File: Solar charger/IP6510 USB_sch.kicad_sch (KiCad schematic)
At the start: 1 part, among them U6 IP6510

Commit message: board compelet
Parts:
- added C17: 22u, Capacitor_SMD:C_0805_2012Metric, symbol Device:C
- added C18: 1u, Capacitor_SMD:C_0805_2012Metric, symbol Device:C
- added C19: 1n, Capacitor_SMD:C_0805_2012Metric, symbol Device:C
- added C20: 0.1u, Capacitor_SMD:C_0805_2012Metric, symbol Device:C
- added C21: 220u, Capacitor_THT:CP_Radial_D6.3mm_P2.50mm, symbol Device:C_Polarized
- added C22: 10u, Capacitor_SMD:C_0805_2012Metric, symbol Device:C
- added L2: L, Inductor_SMD:L_10.4x10.4_H4.8, symbol Device:L
- added R13: 2, Resistor_SMD:R_0805_2012Metric, symbol Device:R_US
- added R14: 3.3k, Resistor_SMD:R_0805_2012Metric, symbol Device:R_US
- U6: footprint Package_SO:SOIC-8-1EP_3.9x4.9mm_P1.27mm_EP2.29x3mm_ThermalVias -> 1Resouce:SOIC-8-1EP_3.9x4.9mm_P1.27mm_EP2.29x3mm_ThermalVias
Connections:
- net GND: now also C17.2, C18.2, C19.2, C21.2, C22.2, R14.2
- net Power Input: now also C17.1, C18.1
- net Power Output: now also C21.1, C22.1, L2.2, R14.1
- net at U6.3 (SW): now also C20.1, L2.1, R13.1
- net at U6.4 (BST): now also C20.2
- new net: C19.1, R13.2

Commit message: 增加新回測報告，單獨IP6050 BOM表
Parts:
- L2: value L -> 22u
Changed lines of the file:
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@@
     (in_bom yes) (on_board yes) (fields_autoplaced)
     (property "Reference" "L2" (id 0) (at 140.97 55.88 90))
-    (property "Value" "L" (id 1) (at 140.97 58.42 90))
+    (property "Value" "22u" (id 1) (at 140.97 58.42 90))
     (property "Footprint" "Inductor_SMD:L_10.4x10.4_H4.8" (id 2) (at 140.97 62.23 0)
       (effects (font (size 1.27 1.27)) hide)
@@
     (pin "1")
   )
+  (sheet_instances
+    (path "/" (page "1"))
+  )
+  (symbol_instances
+    (path "/ec1175d1-1bab-4b8d-ae80-0cf784214bf8"
+      (reference "#PWR07") (unit 1) (value "GND") (footprint "")
+    )
+    (path "/5403a568-63d9-40cc-a753-fb6316d05a55"
+      (reference "C17") (unit 1) (value "22u") (footprint "Capacitor_SMD:C_0805_2012Metric")
+    )
+    (path "/16e5afc8-ff48-4a61-aebb-707d83932b6e"
+      (reference "C18") (unit 1) (value "1u") (footprint "Capacitor_SMD:C_0805_2012Metric")
+    )
+    (path "/c1da5aff-79c8-4d1c-ba9a-24c37276a15a"
+      (reference "C19") (unit 1) (value "1n") (footprint "Capacitor_SMD:C_0805_2012Metric")
+    )
+    (path "/a19c7708-07b9-4e7c-af96-e793517d2808"
+      (reference "C20") (unit 1) (value "0.1u") (footprint "Capacitor_SMD:C_0805_2012Metric")
+    )
+    (path "/4bef6a33-e19b-415f-bbcc-7e54b70d75ed"
+      (reference "C21") (unit 1) (value "220u") (footprint "Capacitor_THT:CP_Radial_D6.3mm_P2.50mm")
+    )
+    (path "/512978ce-74f7-4676-9cdc-95706ce5f098"
+      (reference "C22") (unit 1) (value "10u") (footprint "Capacitor_SMD:C_0805_2012Metric")
+    )
+    (path "/1b7abc99-ad47-483d-8f4a-7ebca9268ba0"
+      (reference "L2") (unit 1) (value "22u") (footprint "Inductor_SMD:L_10.4x10.4_H4.8")
+    )
+    (path "/5b422114-532e-4775-be5f-7c65f529b745"
+      (reference "R13") (unit 1) (value "2") (footprint "Resistor_SMD:R_0805_2012Metric")
+    )
+    (path "/571de38c-5803-4614-b839-1f13c9da8365"
+      (reference "R14") (unit 1) (value "3.3k") (footprint "Resistor_SMD:R_0805_2012Metric")
+    )
+    (path "/2df9c9f8-559b-4185-a144-00c57204afb9"
+      (reference "U6") (unit 1) (value "IP6510") (footprint "1Resouce:SOIC-8-1EP_3.9x4.9mm_P1.27mm_EP2.29x3mm_ThermalVias")
+    )
+  )
 )

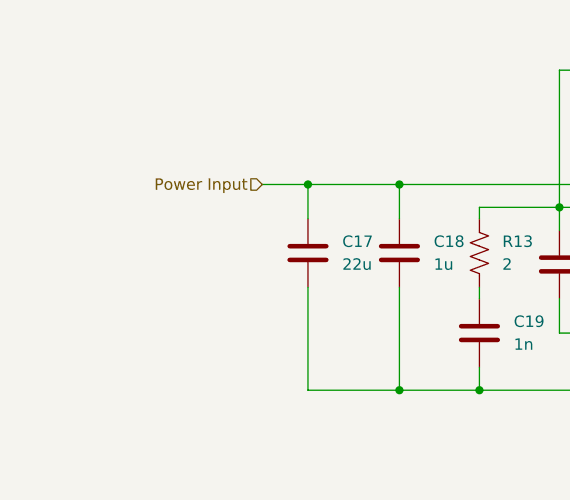
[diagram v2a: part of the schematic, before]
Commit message: 增加電路圖PDF，新增修改一些元件
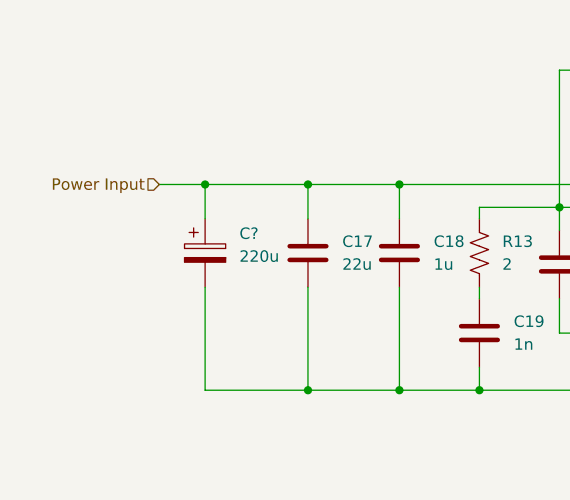
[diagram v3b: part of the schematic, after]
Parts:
- added C?: 220u, Capacitor_THT:CP_Radial_D6.3mm_P2.50mm, symbol Device:C_Polarized
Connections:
- net GND: now also C?.2
- net Power Input: now also C?.1
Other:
- title: (none) -> 8V IN ip6510 Type-c OUT
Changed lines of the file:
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@@
 (kicad_sch (version 20211123) (generator eeschema)
   (paper "A4")
+  (title_block
+    (title "8V IN ip6510 Type-c OUT")
+  )
   (junction (at 146.05 64.77) (diameter 0) (color 0 0 0 0)
   )
+  (junction (at 78.74 97.79) (diameter 0) (color 0 0 0 0)
+  )
   (junction (at 88.9 97.79) (diameter 0) (color 0 0 0 0)
   )
@@
   (junction (at 162.56 97.79) (diameter 0) (color 0 0 0 0)
   )
+  (junction (at 67.31 74.93) (diameter 0) (color 0 0 0 0)
+  )
   (junction (at 162.56 64.77) (diameter 0) (color 0 0 0 0)
   )
@@
     (stroke (width 0) (type default) (color 0 0 0 0))
   )
-  (wire (pts (xy 73.66 74.93) (xy 78.74 74.93))
+  (wire (pts (xy 62.23 74.93) (xy 67.31 74.93))
     (stroke (width 0) (type default) (color 0 0 0 0))
   )
@@
     (stroke (width 0) (type default) (color 0 0 0 0))
   )
+  (wire (pts (xy 67.31 74.93) (xy 78.74 74.93))
+    (stroke (width 0) (type default) (color 0 0 0 0))
+  )
   (wire (pts (xy 88.9 97.79) (xy 97.79 97.79))
     (stroke (width 0) (type default) (color 0 0 0 0))
@@
     (stroke (width 0) (type default) (color 0 0 0 0))
   )
+  (wire (pts (xy 67.31 86.36) (xy 67.31 97.79))
+    (stroke (width 0) (type default) (color 0 0 0 0))
+  )
   (wire (pts (xy 146.05 64.77) (xy 151.13 64.77))
     (stroke (width 0) (type default) (color 0 0 0 0))
@@
     (stroke (width 0) (type default) (color 0 0 0 0))
   )
+  (wire (pts (xy 67.31 74.93) (xy 67.31 78.74))
+    (stroke (width 0) (type default) (color 0 0 0 0))
+  )
   (wire (pts (xy 172.72 64.77) (xy 177.8 64.77))
     (stroke (width 0) (type default) (color 0 0 0 0))
@@
     (stroke (width 0) (type default) (color 0 0 0 0))
   )
+  (wire (pts (xy 67.31 97.79) (xy 78.74 97.79))
+    (stroke (width 0) (type default) (color 0 0 0 0))
+  )
   (wire (pts (xy 106.68 77.47) (xy 106.68 62.23))
     (stroke (width 0) (type default) (color 0 0 0 0))
@@
     (stroke (width 0) (type default) (color 0 0 0 0))
   )
-  (hierarchical_label "Power Input" (shape input) (at 73.66 74.93 180)
+  (hierarchical_label "Power Input" (shape input) (at 62.23 74.93 180)
     (effects (font (size 1.27 1.27)) (justify right))
   )
@@
     (pin "1")
   )
+  (symbol (lib_id "Device:C_Polarized") (at 67.31 82.55 0) (unit 1)
+    (in_bom yes) (on_board yes) (fields_autoplaced)
+    (property "Reference" "C?" (id 0) (at 71.12 80.3909 0)
+      (effects (font (size 1.27 1.27)) (justify left))
+    )
+    (property "Value" "220u" (id 1) (at 71.12 82.9309 0)
+      (effects (font (size 1.27 1.27)) (justify left))
+    )
+    (property "Footprint" "Capacitor_THT:CP_Radial_D6.3mm_P2.50mm" (id 2) (at 68.2752 86.36 0)
+      (effects (font (size 1.27 1.27)) hide)
+    )
+    (property "Datasheet" "~" (id 3) (at 67.31 82.55 0)
+      (effects (font (size 1.27 1.27)) hide)
+    )
+    (pin "1")
+    (pin "2")
+  )
   (sheet_instances
